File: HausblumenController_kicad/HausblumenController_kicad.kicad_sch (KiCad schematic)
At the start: 25 parts, among them Q1 IRF520N, Q2 IRF520N, Q3 IRF520N, Q4 IRLML0030, SW1 RotaryEncoder_Switch_MP, U1 BlackPill_40pin_SWD, U2 BME280

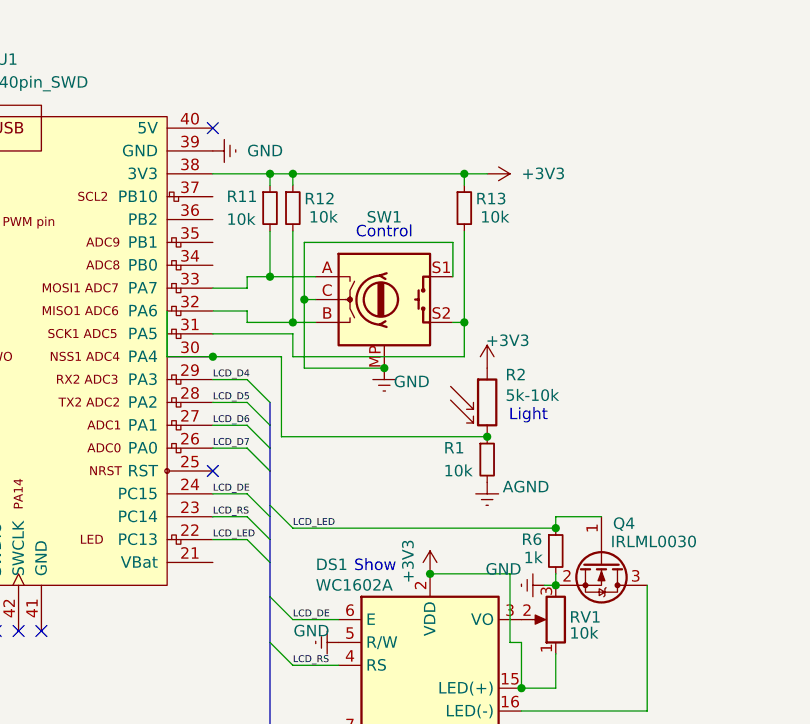
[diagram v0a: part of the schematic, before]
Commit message: feat: configure CubeMX
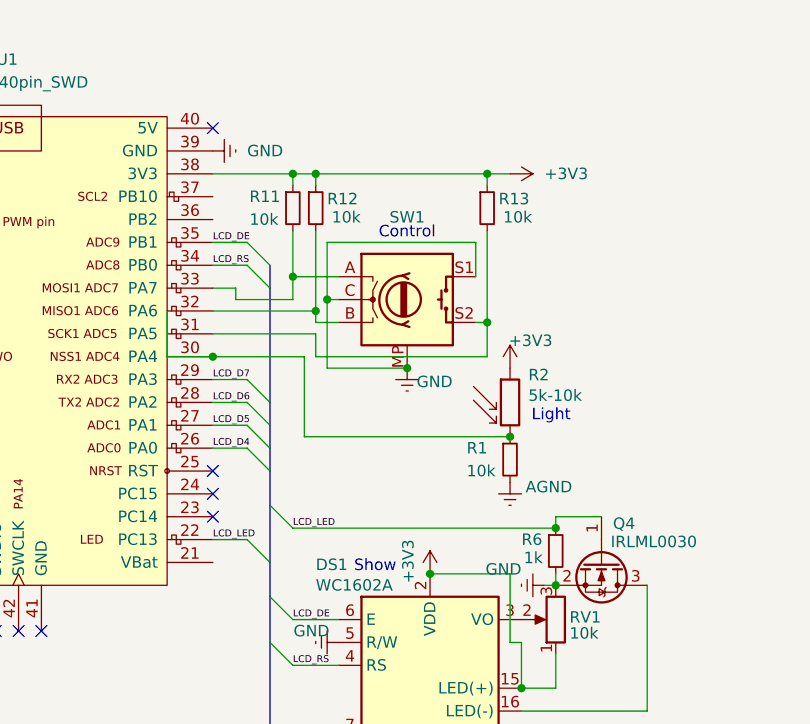
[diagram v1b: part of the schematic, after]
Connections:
- net LCD_D4: now also U1.26 (PA0); no longer U1.29 (PA3)
- net LCD_D5: now also U1.27 (PA1); no longer U1.28 (PA2)
- net LCD_D6: now also U1.28 (PA2); no longer U1.27 (PA1)
- net LCD_D7: now also U1.29 (PA3); no longer U1.26 (PA0)
- net LCD_DE: now also U1.35 (PB1); no longer U1.24 (PC15)
- net LCD_RS: now also U1.34 (PB0); no longer U1.23 (PC14)
- no-connect marks 16 -> 18
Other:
- moved on the sheet: R1, R11, R12, R13, R2, SW1

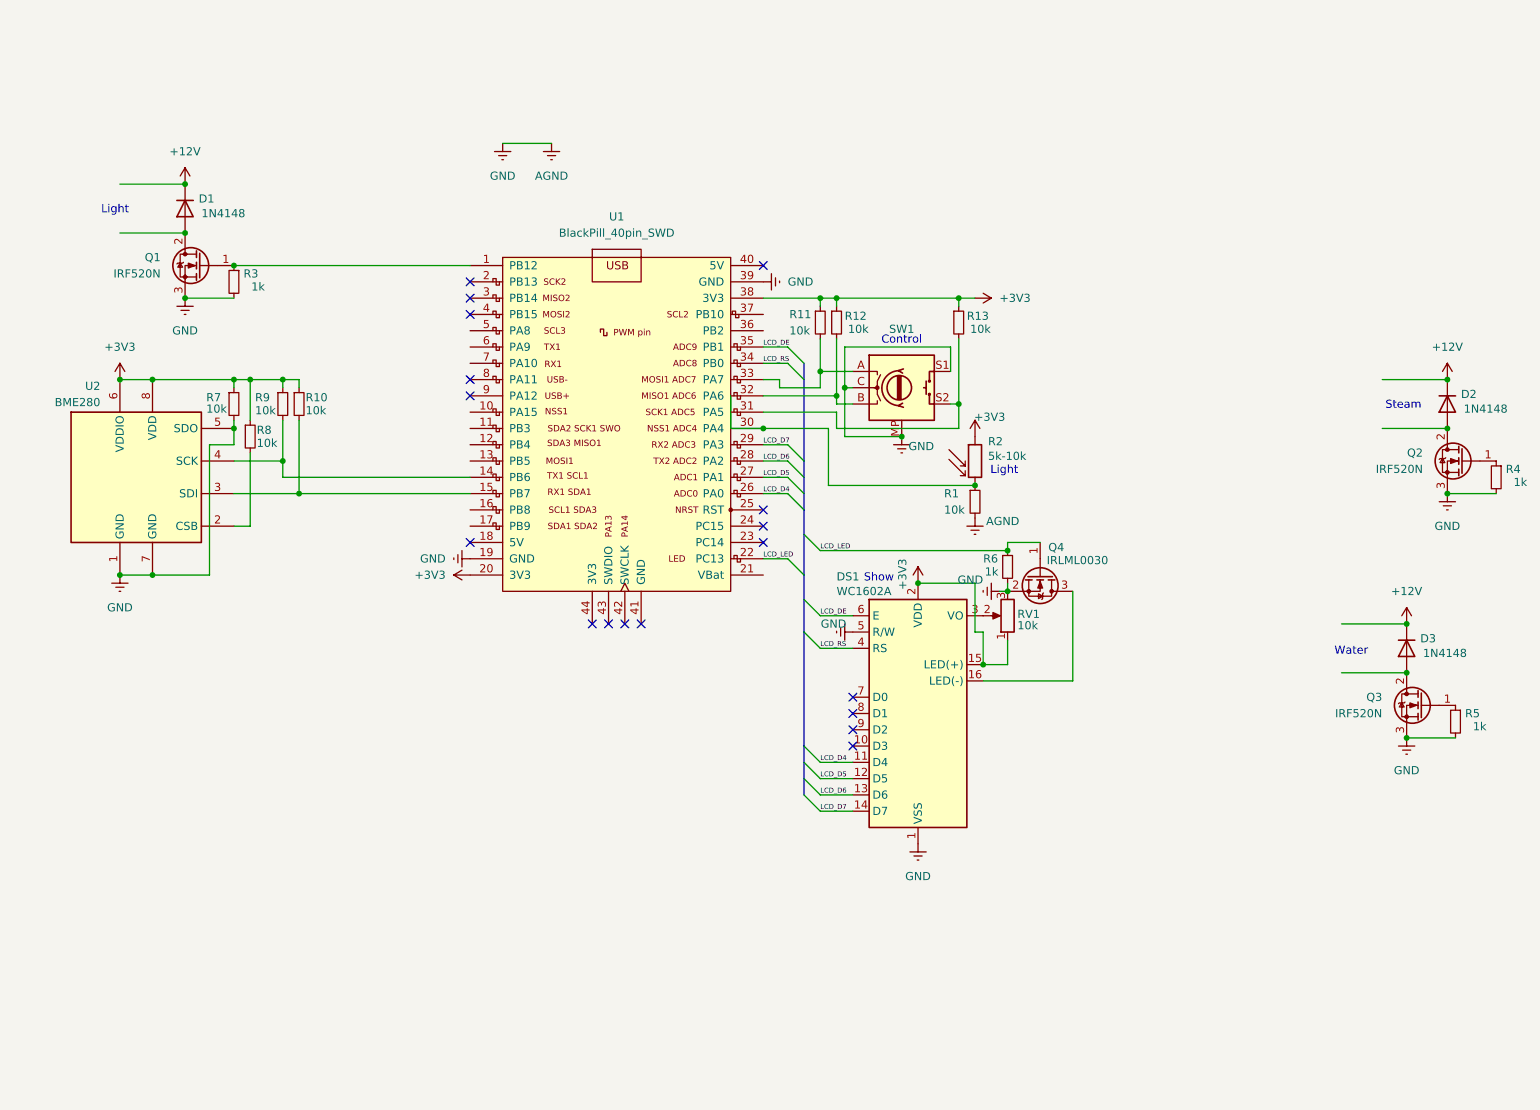
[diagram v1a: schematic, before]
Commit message: feat: added power circuit
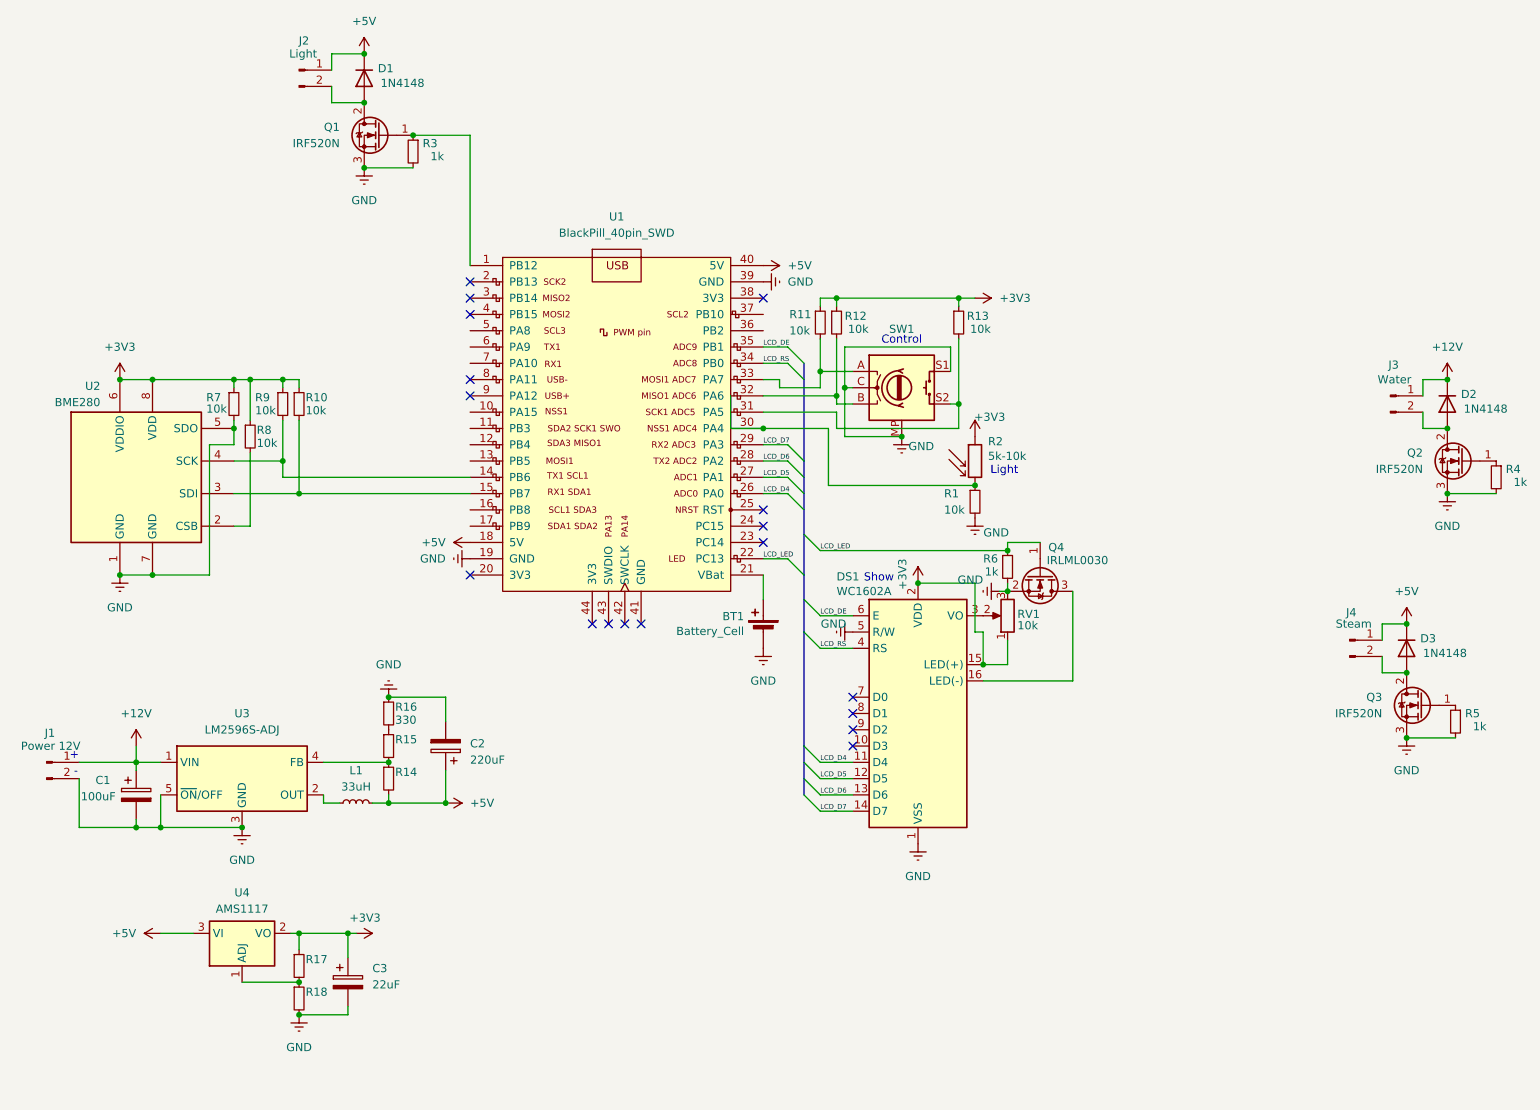
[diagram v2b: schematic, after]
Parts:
- added BT1: Battery_Cell, librarise:BAT-SMD_CR1220-2, symbol Device:Battery_Cell
- added C1: 100uF, Capacitor_SMD:CP_Elec_6.3x7.7, symbol Device:C_Polarized
- added C2: 220uF, Capacitor_SMD:CP_Elec_6.3x7.7, symbol Device:C_Polarized
- added C3: 22uF, Capacitor_SMD:CP_Elec_6.3x5.7, symbol Device:C_Polarized
- added J1: Power 12V, Connector_PinHeader_2.54mm:PinHeader_1x02_P2.54mm_Vertical, symbol Connector:Conn_01x02_Pin
- added J2: Light, Connector_PinHeader_2.54mm:PinHeader_1x02_P2.54mm_Vertical, symbol Connector:Conn_01x02_Pin
- added J3: Water, Connector_PinHeader_2.54mm:PinHeader_1x02_P2.54mm_Vertical, symbol Connector:Conn_01x02_Pin
- added J4: Steam, Connector_PinHeader_2.54mm:PinHeader_1x02_P2.54mm_Vertical, symbol Connector:Conn_01x02_Pin
- added L1: 33uH, Inductor_SMD:L_Ferrocore_DLG-0504, symbol Device:L_Small
- added R14, R15, R17, R18: ~, Resistor_SMD:R_0603_1608Metric, symbol Device:R_Small
- added R16: 330, Resistor_SMD:R_0603_1608Metric, symbol Device:R_Small
- added U3: LM2596S-ADJ, Package_TO_SOT_SMD:TO-263-5_TabPin3, symbol Regulator_Switching:LM2596S-ADJ
- added U4: AMS1117, Package_TO_SOT_SMD:SOT-223-3_TabPin2, symbol Regulator_Linear:AMS1117
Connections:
- net +12V: now also C1.1, J1.1 (Pin_1), J3.1 (Pin_1), U3.1 (VIN); no longer D1.1 (K), D3.1 (K)
- net +3V3: now also C3.1, R17.1, U4.2 (VO); no longer U1.20 (3V3), U1.38 (3V3)
- net +5V: now reaches U1.18 (5V)
- net +5V: now also D1.1 (K), D3.1 (K), U1.40 (5V), C2.1, J2.1 (Pin_1), J4.1 (Pin_1), L1.2, R14.2, U4.3 (VI)
- net at U1.21 (VBat): now also BT1.1 (+)
- net at D1.2 (A), Q1.2 (D): now also J2.2 (Pin_2)
- net at D3.2 (A), Q3.2 (D): now also J4.2 (Pin_2)
- net at D2.2 (A), Q2.2 (D): now also J3.2 (Pin_2)
- net AGND renamed GND
- net GND: now also BT1.2 (-), C1.2, C2.2, C3.2, J1.2 (Pin_2), R16.1, R18.2, U3.3 (GND), U3.5 (~{ON}/OFF)
- new net: R17.2, R18.1, U4.1 (ADJ)
- new net: L1.1, U3.2 (OUT)
- new net: R14.1, R15.2, U3.4 (FB)
- new net: R15.1, R16.2
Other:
- note added: "+"
- note added: "-"
- note removed: "Steam"
- note removed: "Water"
- moved on the sheet: D1, Q1, R3

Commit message: chore: naming GPIO
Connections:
- net at Q2.1 (G), R4.1: now also U1.13 (PB5)
- net at U1.12 (PB4): now also Q3.1 (G), R5.1
- no-connect marks 18 -> 19
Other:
- moved on the sheet: BT1, C1, C2, C3, D1, D2, D3, DS1, J1, J2, J3, J4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

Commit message: chore: selected resistor div
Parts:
- removed R16: 330, Resistor_SMD:R_0603_1608Metric, symbol Device:R_Small
- R14: value ~ -> 7,6k
- R15: value ~ -> 2,4k
- R17: value ~ -> 6,2k
- R18: value ~ -> 3,8k
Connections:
- net GND: now also R15.1
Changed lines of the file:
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@@
 	)
 	(junction
+		(at 109.22 125.73)
+		(diameter 0)
+		(color 0 0 0 0)
+	)
+	(junction
 		(at 93.98 41.91)
 		(diameter 0)
@@
 	)
 	(junction
-		(at 109.22 121.92)
-		(diameter 0)
-		(color 0 0 0 0)
-	)
-	(junction
 		(at 68.58 52.07)
 		(diameter 0)
@@
 	(wire
 		(pts
-			(xy 118.11 125.73) (xy 118.11 121.92)
+			(xy 97.79 93.98) (xy 95.25 93.98)
 		)
 		(stroke
@@
 	(wire
 		(pts
-			(xy 97.79 93.98) (xy 95.25 93.98)
+			(xy 186.69 64.77) (xy 186.69 69.85)
 		)
 		(stroke
@@
 	(wire
 		(pts
-			(xy 186.69 64.77) (xy 186.69 69.85)
+			(xy 93.98 34.29) (xy 90.17 34.29)
 		)
 		(stroke
@@
 	(wire
 		(pts
-			(xy 93.98 34.29) (xy 90.17 34.29)
+			(xy 90.17 34.29) (xy 90.17 36.83)
 		)
 		(stroke
@@
 	(wire
 		(pts
-			(xy 90.17 34.29) (xy 90.17 36.83)
+			(xy 64.77 34.29) (xy 64.77 36.83)
 		)
 		(stroke
@@
 	(wire
 		(pts
-			(xy 64.77 34.29) (xy 64.77 36.83)
+			(xy 95.25 81.28) (xy 95.25 78.74)
 		)
 		(stroke
@@
 	(wire
 		(pts
-			(xy 95.25 81.28) (xy 95.25 78.74)
+			(xy 186.69 69.85) (xy 191.77 69.85)
 		)
 		(stroke
@@
 	(wire
 		(pts
-			(xy 186.69 69.85) (xy 191.77 69.85)
+			(xy 109.22 125.73) (xy 109.22 127)
 		)
 		(stroke
@@
 	(wire
 		(pts
-			(xy 118.11 121.92) (xy 109.22 121.92)
+			(xy 118.11 125.73) (xy 109.22 125.73)
 		)
 		(stroke
@@
 		)
 	)
+	(wire
+		(pts
+			(xy 109.22 125.73) (xy 109.22 124.46)
+		)
+		(stroke
+			(width 0)
+			(type default)
+		)
+	)
+	(text_box "1V25"
+		(exclude_from_sim no)
+		(at 87.63 171.45 0)
+		(size 6.35 3.81)
+		(stroke
+			(width 0)
+			(type default)
+		)
+		(fill
+			(type none)
+		)
+		(effects
+			(font
+				(size 1.27 1.27)
+			)
+			(justify left top)
+		)
+	)
+	(text_box "1V23"
+		(exclude_from_sim no)
+		(at 100.33 127 0)
+		(size 6.35 3.81)
+		(stroke
+			(width 0)
+			(type default)
+		)
+		(fill
+			(type none)
+		)
+		(effects
+			(font
+				(size 1.27 1.27)
+			)
+			(justify left top)
+		)
+	)
 	(text "+\n"
 		(exclude_from_sim no)
@@
 	)
 	(symbol
-		(lib_id "Device:R_Small")
-		(at 109.22 124.46 0)
-		(unit 1)
-		(exclude_from_sim no)
-		(in_bom yes)
-		(on_board yes)
-		(dnp no)
-		(property "Reference" "R16"
-			(at 110.236 123.444 0)
-			(effects
-				(font
-					(size 1.27 1.27)
-				)
-				(justify left)
-			)
-		)
-		(property "Value" "330"
-			(at 110.236 125.476 0)
-			(effects
-				(font
-					(size 1.27 1.27)
-				)
-				(justify left)
-			)
-		)
-		(property "Footprint" "Resistor_SMD:R_0603_1608Metric"
-			(at 109.22 124.46 0)
-			(effects
-				(font
-					(size 1.27 1.27)
-				)
-				(hide yes)
-			)
-		)
-		(property "Datasheet" "~"
-			(at 109.22 124.46 0)
-			(effects
-				(font
-					(size 1.27 1.27)
-				)
-				(hide yes)
-			)
-		)
-		(property "Description" "Resistor, small symbol"
-			(at 109.22 124.46 0)
-			(effects
-				(font
-					(size 1.27 1.27)
-				)
-				(hide yes)
-			)
-		)
-		(pin "2"
-		)
-		(pin "1"
-		)
-		(instances
-			(project "HausblumenController_kicad"
-				(path "/763b7ff5-a573-497b-9e68-3c06692609a4"
-					(reference "R16")
-					(unit 1)
-				)
-			)
-		)
-	)
-	(symbol
 		(lib_id "power:+3V3")
 		(at 201.93 102.87 0)
@@
 			)
 		)
-		(property "Value" "~"
+		(property "Value" "3,8k"
 			(at 96.266 173.736 0)
 			(effects
@@
 			)
 		)
-		(property "Value" "~"
+		(property "Value" "7,6k"
 			(at 110.236 135.636 0)
 			(effects
@@
 	(symbol
 		(lib_id "power:Earth")
-		(at 109.22 121.92 180)
+		(at 109.22 124.46 180)
 		(unit 1)
 		(exclude_from_sim no)
@@
 		(fields_autoplaced yes)
 		(property "Reference" "#PWR014"
-			(at 109.22 115.57 0)
+			(at 109.22 118.11 0)
 			(effects
 				(font
@@
 		)
 		(property "Value" "GND"
-			(at 109.22 116.84 0)
+			(at 109.22 119.38 0)
 			(effects
 				(font
@@
 		)
 		(property "Footprint" ""
-			(at 109.22 121.92 0)
+			(at 109.22 124.46 0)
 			(effects
 				(font
@@
 		)
 		(property "Datasheet" "~"
-			(at 109.22 121.92 0)
+			(at 109.22 124.46 0)
 			(effects
 				(font
@@
 		)
 		(property "Description" "Power symbol creates a global label with name \"Earth\""
-			(at 109.22 121.92 0)
+			(at 109.22 124.46 0)
 			(effects
 				(font
@@
 			)
 		)
-		(property "Value" "~"
+		(property "Value" "6,2k"
 			(at 96.266 168.656 0)
 			(effects
@@
 			)
 		)
-		(property "Value" "~"
+		(property "Value" "2,4k"
 			(at 110.236 130.556 0)
 			(effects

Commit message: fix: update encoder mode
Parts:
- R14: value 7,6k -> 7,5k
- R18: value 3,8k -> 3,9k
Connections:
- net +3V3: no longer DS1.15 (LED(+)), DS1.2 (VDD), RV1.1
- net +5V: now also DS1.15 (LED(+)), DS1.2 (VDD), RV1.1
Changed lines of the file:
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@@
 			)
 		)
-		(property "Value" "+3V3"
+		(property "Value" "+5V"
 			(at 199.517 101.473 90)
 			(effects
@@
 			)
 		)
-		(property "Value" "3,8k"
+		(property "Value" "3,9k"
 			(at 96.266 173.736 0)
 			(effects
@@
 			)
 		)
-		(property "Value" "7,6k"
+		(property "Value" "7,5k"
 			(at 110.236 135.636 0)
 			(effects

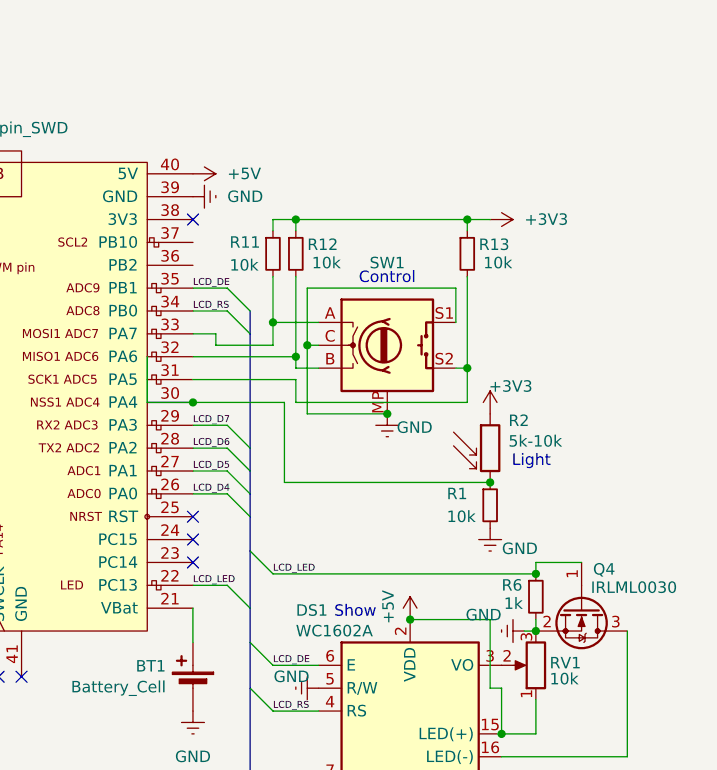
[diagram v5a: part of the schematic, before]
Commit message: fix: capacitor and programm filtr encoder
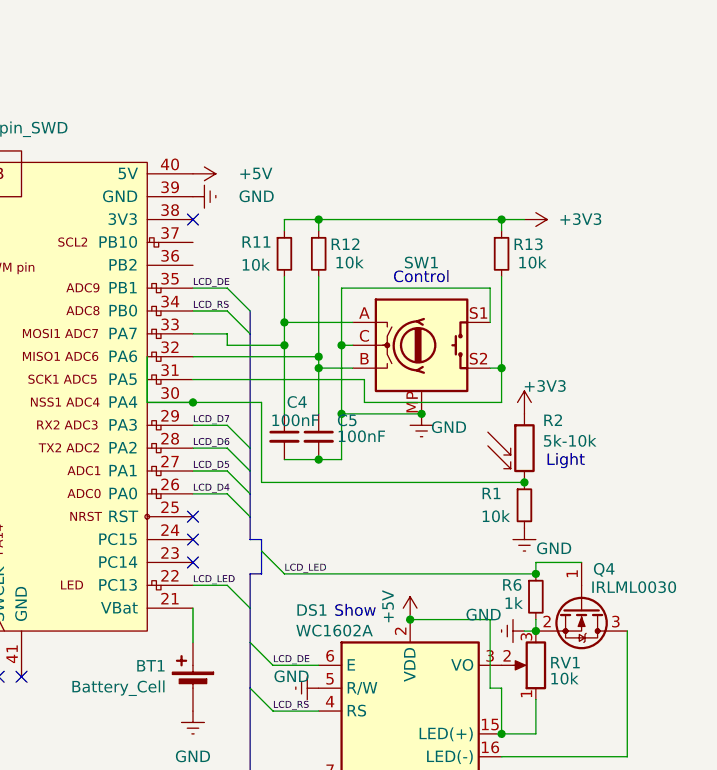
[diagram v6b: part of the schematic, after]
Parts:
- added C4, C5: 100nF, Capacitor_SMD:C_0402_1005Metric, symbol Device:C_Small
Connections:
- net GND: now also C4.2, C5.2
- net at R12.2, SW1.B, U1.32 (PA6): now also C5.1
- net at R11.2, SW1.A, U1.33 (PA7): now also C4.1
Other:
- moved on the sheet: R1, R11, R12, R13, R2, SW1
